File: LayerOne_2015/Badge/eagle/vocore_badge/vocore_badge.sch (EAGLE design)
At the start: 19 parts

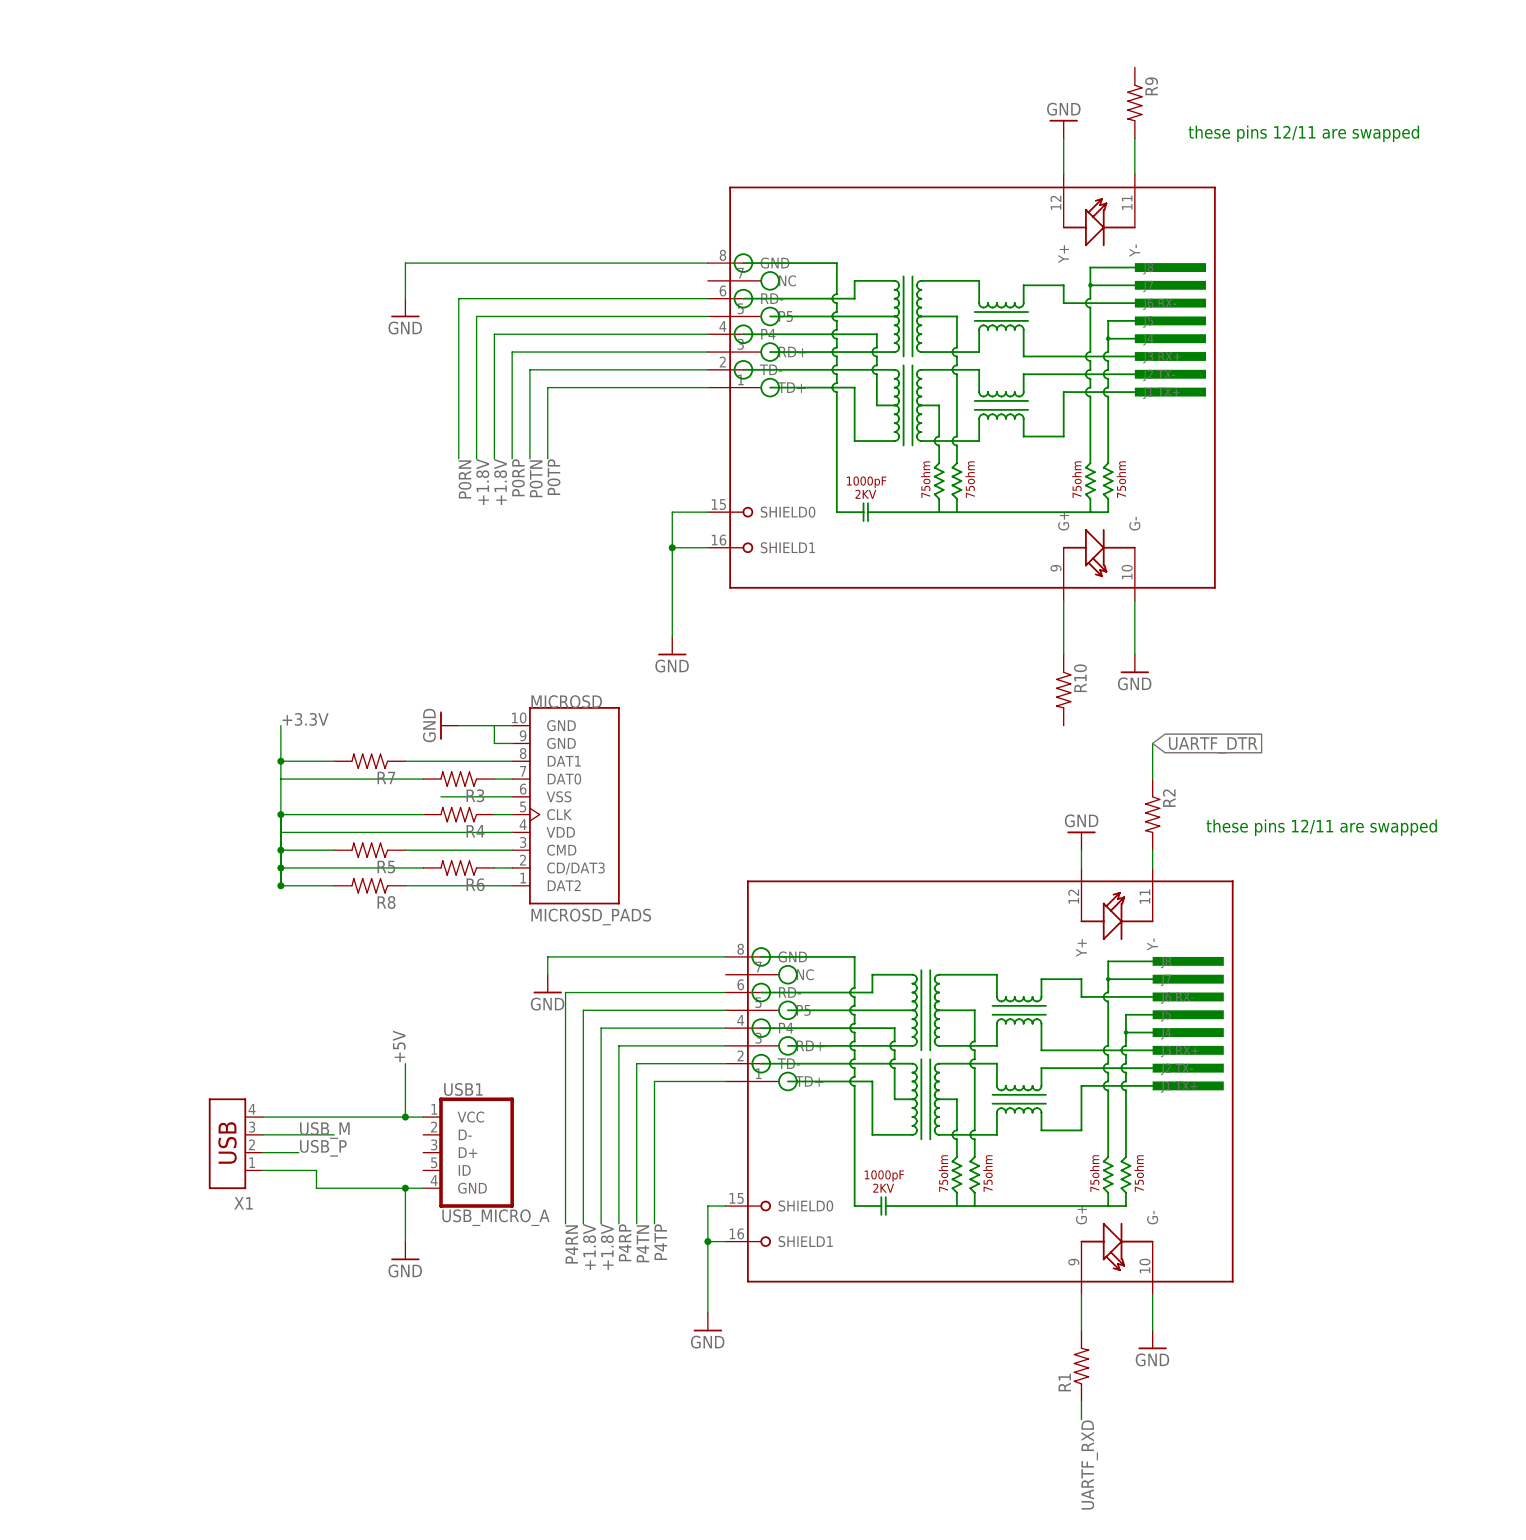
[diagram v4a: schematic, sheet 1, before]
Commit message: elongated pads on 245 logic convertor
fixed usb on badge
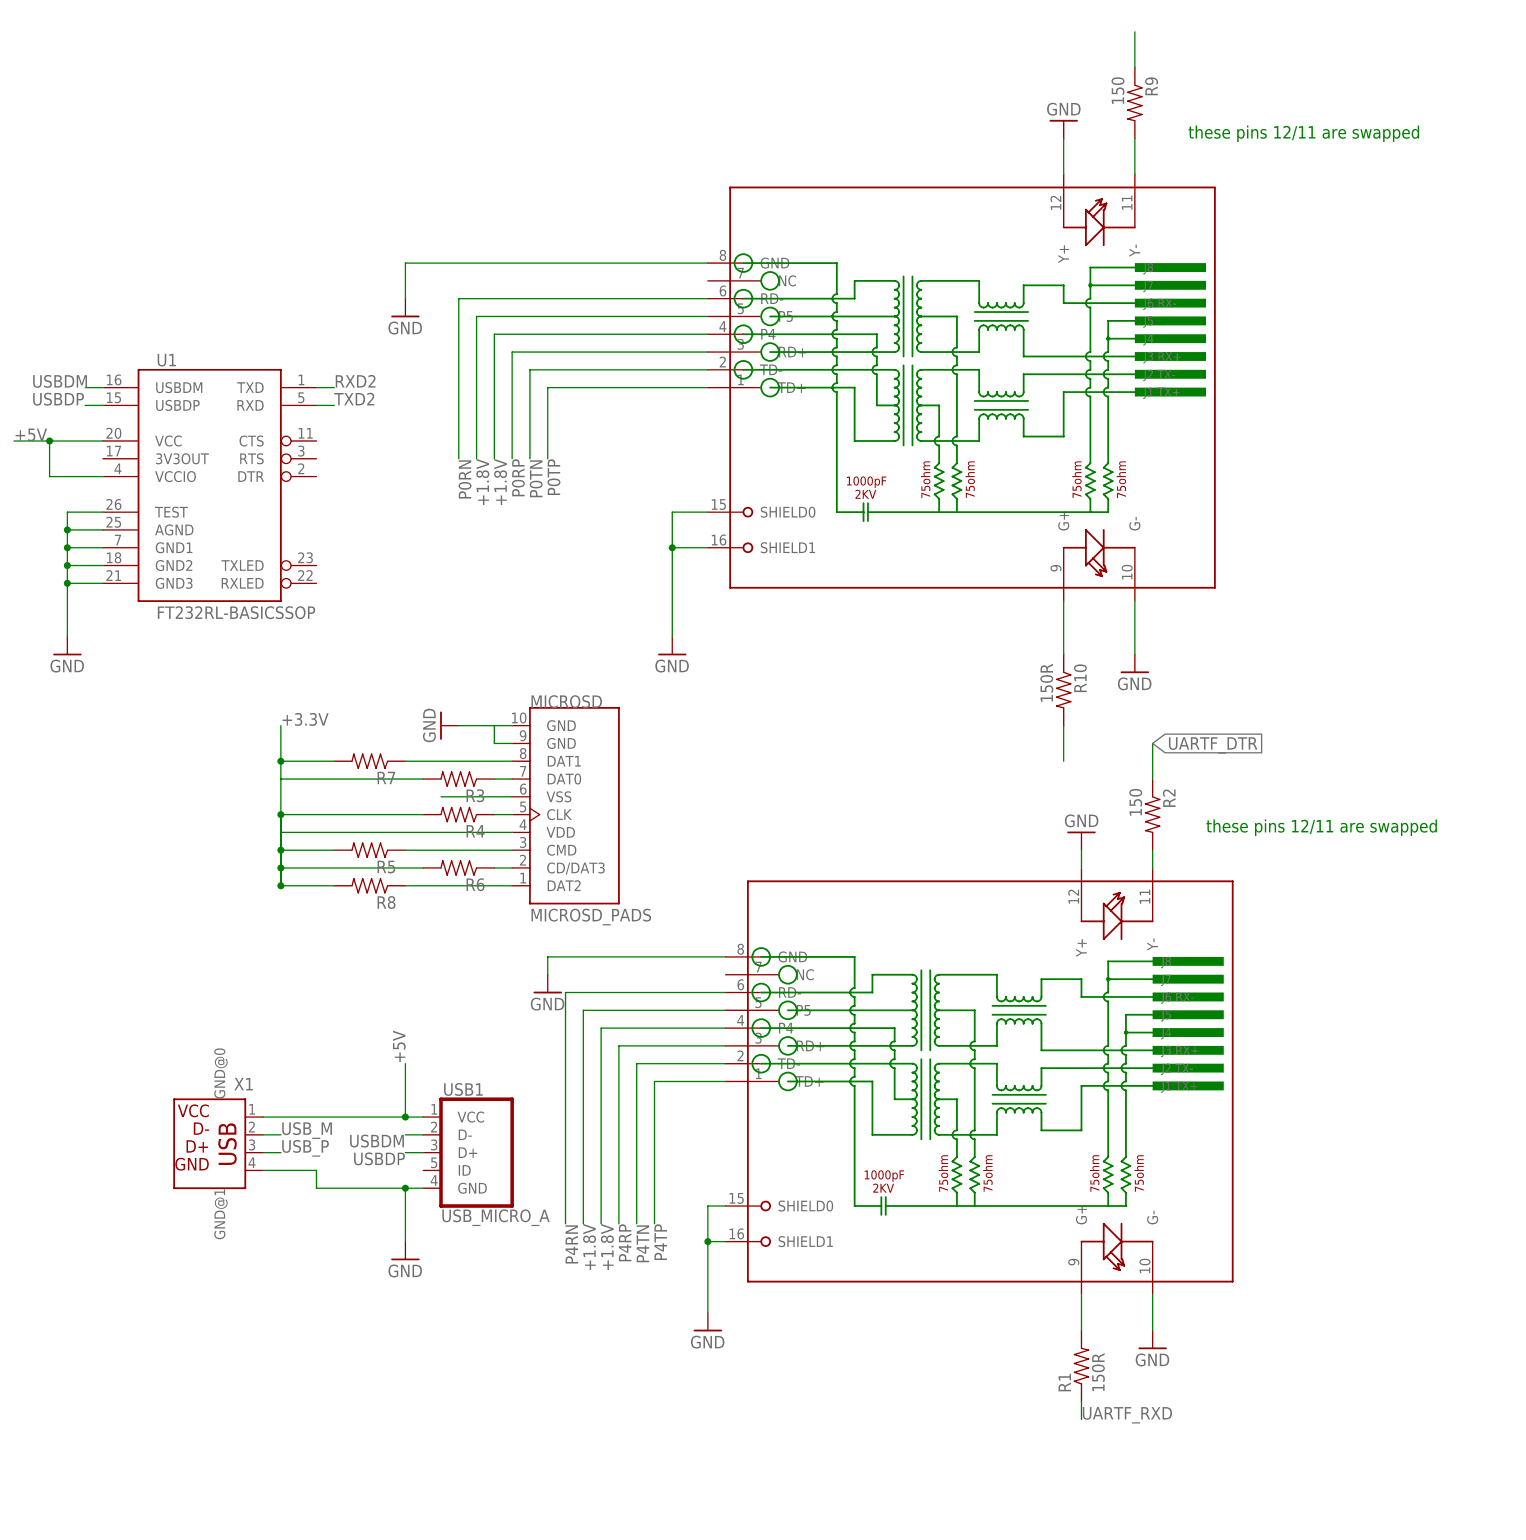
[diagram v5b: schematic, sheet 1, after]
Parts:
- added JP4: (no value), adafruit:PINHD-1X3
- added JP5: (no value), pinhead:PINHD-1X2
- added U1: FT232RL-BASICSSOP, SparkFun:FT232RL-BASICSSOP
- R1, R10: value (none) -> 150R
- R2, R9: value (none) -> 150
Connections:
- new net N$6: R9.1
- new net N$7: R10.2
- new net USBDM: U1.USBDM, USB1.D-
- new net USBDP: U1.USBDP, USB1.D+
- net +5V: now also JP5.2, U1.VCC, U1.VCCIO, X1.1; no longer X1.4
- net GND: now also JP4.1, JP5.1, U1.AGND, U1.GND1, U1.GND2, U1.GND3, U1.TEST, X1.4; no longer X1.1
- net RXD2: now also JP4.2, U1.TXD
- net TXD2: now also JP4.3, U1.RXD
- net USB_M: now also X1.2; no longer X1.3
- net USB_P: now also X1.3; no longer X1.2
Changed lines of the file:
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@@
 <classes>
 <class number="0" name="default" width="0.254" drill="0">
+<clearance class="0" value="0.1524"/>
 </class>
 </classes>
@@
 <part name="GND2" library="supply1" deviceset="GND" device=""/>
 <part name="GND3" library="supply1" deviceset="GND" device=""/>
-<part name="R1" library="SparkFun-Resistors" deviceset="RESISTOR" device="0805-RES"/>
-<part name="R2" library="SparkFun-Resistors" deviceset="RESISTOR" device="0805-RES"/>
+<part name="R1" library="SparkFun-Resistors" deviceset="RESISTOR" device="0805-RES" value="150R"/>
+<part name="R2" library="SparkFun-Resistors" deviceset="RESISTOR" device="0805-RES" value="150"/>
 <part name="R3" library="SparkFun-Resistors" deviceset="RESISTOR" device="0805-RES"/>
 <part name="R4" library="SparkFun-Resistors" deviceset="RESISTOR" device="0805-RES"/>
@@
 <part name="GND10" library="supply1" deviceset="GND" device=""/>
 <part name="GND11" library="supply1" deviceset="GND" device=""/>
-<part name="R9" library="SparkFun-Resistors" deviceset="RESISTOR" device="0805-RES"/>
-<part name="R10" library="SparkFun-Resistors" deviceset="RESISTOR" device="0805-RES"/>
-<part name="X1" library="con-amp" deviceset="USB-787616" device=""/>
+<part name="R9" library="SparkFun-Resistors" deviceset="RESISTOR" device="0805-RES" value="150"/>
+<part name="R10" library="SparkFun-Resistors" deviceset="RESISTOR" device="0805-RES" value="150R"/>
 <part name="JP1" library="adafruit" deviceset="PINHD-1X14" device=""/>
 <part name="JP2" library="adafruit" deviceset="PINHD-1X14" device=""/>
 <part name="JP3" library="microbuilder" deviceset="HEADER-1X7" device="ROUND"/>
+<part name="U1" library="SparkFun" deviceset="FT232RL-BASIC" device="SSOP"/>
+<part name="GND12" library="supply1" deviceset="GND" device=""/>
+<part name="JP4" library="adafruit" deviceset="PINHD-1X3" device=""/>
+<part name="JP5" library="pinhead" deviceset="PINHD-1X2" device=""/>
+<part name="X1" library="con-amp" deviceset="USB-787616" device=""/>
 </parts>
 <sheets>
@@
 <instance part="R9" gate="G$1" x="-93.98" y="226.06" rot="R270"/>
 <instance part="R10" gate="G$1" x="-104.14" y="142.24" rot="R270"/>
-<instance part="X1" gate="G$1" x="-223.52" y="78.74" rot="R180"/>
+<instance part="U1" gate="G$1" x="-226.06" y="172.72"/>
+<instance part="GND12" gate="1" x="-246.38" y="147.32"/>
+<instance part="X1" gate="G$1" x="-223.52" y="76.2" rot="MR0"/>
 </instances>
 <busses>
@@
 <wire x1="-210.82" y1="71.12" x2="-210.82" y2="73.66" width="0.1524" layer="91"/>
 <junction x="-198.12" y="71.12"/>
-<pinref part="X1" gate="G$1" pin="1"/>
+<pinref part="X1" gate="G$1" pin="4"/>
 </segment>
 <segment>
@@
 <pinref part="GND11" gate="1" pin="GND"/>
 </segment>
+<segment>
+<pinref part="U1" gate="G$1" pin="GND1"/>
+<wire x1="-241.3" y1="162.56" x2="-246.38" y2="162.56" width="0.1524" layer="91"/>
+<wire x1="-246.38" y1="162.56" x2="-246.38" y2="160.02" width="0.1524" layer="91"/>
+<pinref part="U1" gate="G$1" pin="GND2"/>
+<wire x1="-246.38" y1="160.02" x2="-246.38" y2="157.48" width="0.1524" layer="91"/>
+<wire x1="-246.38" y1="157.48" x2="-246.38" y2="149.86" width="0.1524" layer="91"/>
+<wire x1="-241.3" y1="160.02" x2="-246.38" y2="160.02" width="0.1524" layer="91"/>
+<pinref part="U1" gate="G$1" pin="GND3"/>
+<wire x1="-241.3" y1="157.48" x2="-246.38" y2="157.48" width="0.1524" layer="91"/>
+<junction x="-246.38" y="157.48"/>
+<junction x="-246.38" y="160.02"/>
+<pinref part="U1" gate="G$1" pin="AGND"/>
+<wire x1="-241.3" y1="165.1" x2="-246.38" y2="165.1" width="0.1524" layer="91"/>
+<wire x1="-246.38" y1="165.1" x2="-246.38" y2="162.56" width="0.1524" layer="91"/>
+<pinref part="GND12" gate="1" pin="GND"/>
+<pinref part="U1" gate="G$1" pin="TEST"/>
+<wire x1="-241.3" y1="167.64" x2="-246.38" y2="167.64" width="0.1524" layer="91"/>
+<wire x1="-246.38" y1="167.64" x2="-246.38" y2="165.1" width="0.1524" layer="91"/>
+<junction x="-246.38" y="162.56"/>
+<junction x="-246.38" y="165.1"/>
+</segment>
 </net>
 <net name="LED_G" class="0">
@@
 <pinref part="R1" gate="G$1" pin="1"/>
 <wire x1="-101.6" y1="40.64" x2="-101.6" y2="38.1" width="0.1524" layer="91"/>
-<label x="-101.6" y="38.1" size="1.778" layer="95" rot="R270"/>
+<label x="-101.6" y="38.1" size="1.778" layer="95"/>
 </segment>
 </net>
@@
 <wire x1="-218.44" y1="81.28" x2="-198.12" y2="81.28" width="0.1524" layer="91"/>
 <junction x="-198.12" y="81.28"/>
-<pinref part="X1" gate="G$1" pin="4"/>
+<pinref part="X1" gate="G$1" pin="1"/>
+</segment>
+<segment>
+<pinref part="U1" gate="G$1" pin="VCCIO"/>
+<wire x1="-241.3" y1="172.72" x2="-248.92" y2="172.72" width="0.1524" layer="91"/>
+<wire x1="-248.92" y1="172.72" x2="-248.92" y2="177.8" width="0.1524" layer="91"/>
+<pinref part="U1" gate="G$1" pin="VCC"/>
+<wire x1="-248.92" y1="177.8" x2="-254" y2="177.8" width="0.1524" layer="91"/>
+<wire x1="-241.3" y1="177.8" x2="-248.92" y2="177.8" width="0.1524" layer="91"/>
+<junction x="-248.92" y="177.8"/>
+<label x="-254" y="177.8" size="1.778" layer="95"/>
 </segment>
 </net>
 <net name="USB_P" class="0">
 <segment>
-<wire x1="-218.44" y1="76.2" x2="-213.36" y2="76.2" width="0.1524" layer="91"/>
-<label x="-213.36" y="76.2" size="1.778" layer="95"/>
+<wire x1="-218.44" y1="76.2" x2="-215.9" y2="76.2" width="0.1524" layer="91"/>
+<label x="-215.9" y="76.2" size="1.778" layer="95"/>
+<pinref part="X1" gate="G$1" pin="3"/>
+</segment>
+</net>
+<net name="USB_M" class="0">
+<segment>
+<wire x1="-218.44" y1="78.74" x2="-215.9" y2="78.74" width="0.1524" layer="91"/>
+<label x="-215.9" y="78.74" size="1.778" layer="95"/>
 <pinref part="X1" gate="G$1" pin="2"/>
-</segment>
-</net>
-<net name="USB_M" class="0">
-<segment>
-<wire x1="-218.44" y1="78.74" x2="-208.28" y2="78.74" width="0.1524" layer="91"/>
-<label x="-213.36" y="78.74" size="1.778" layer="95"/>
-<pinref part="X1" gate="G$1" pin="3"/>
 </segment>
 </net>
@@
 </segment>
 </net>
+<net name="USBDM" class="0">
+<segment>
+<pinref part="USB1" gate="G$1" pin="D-"/>
+<wire x1="-195.58" y1="78.74" x2="-198.12" y2="78.74" width="0.1524" layer="91"/>
+<label x="-198.12" y="78.74" size="1.778" layer="95" rot="R180"/>
+</segment>
+<segment>
+<wire x1="-241.3" y1="185.42" x2="-243.84" y2="185.42" width="0.1524" layer="91"/>
+<pinref part="U1" gate="G$1" pin="USBDM"/>
+<label x="-251.46" y="185.42" size="1.778" layer="95"/>
+</segment>
+</net>
+<net name="USBDP" class="0">
+<segment>
+<pinref part="USB1" gate="G$1" pin="D+"/>
+<wire x1="-195.58" y1="76.2" x2="-198.12" y2="76.2" width="0.1524" layer="91"/>
+<label x="-198.12" y="76.2" size="1.778" layer="95" rot="R180"/>
+</segment>
+<segment>
+<wire x1="-241.3" y1="182.88" x2="-243.84" y2="182.88" width="0.1524" layer="91"/>
+<pinref part="U1" gate="G$1" pin="USBDP"/>
+<label x="-251.46" y="182.88" size="1.778" layer="95"/>
+</segment>
+</net>
+<net name="RXD2" class="0">
+<segment>
+<pinref part="U1" gate="G$1" pin="TXD"/>
+<wire x1="-210.82" y1="185.42" x2="-208.28" y2="185.42" width="0.1524" layer="91"/>
+<label x="-208.28" y="185.42" size="1.778" layer="95"/>
+</segment>
+</net>
+<net name="TXD2" class="0">
+<segment>
+<pinref part="U1" gate="G$1" pin="RXD"/>
+<wire x1="-210.82" y1="182.88" x2="-208.28" y2="182.88" width="0.1524" layer="91"/>
+<label x="-208.28" y="182.88" size="1.778" layer="95"/>
+</segment>
+</net>
+<net name="N$6" class="0">
+<segment>
+<pinref part="R9" gate="G$1" pin="1"/>
+<wire x1="-93.98" y1="231.14" x2="-93.98" y2="236.22" width="0.1524" layer="91"/>
+</segment>
+</net>
+<net name="N$7" class="0">
+<segment>
+<pinref part="R10" gate="G$1" pin="2"/>
+<wire x1="-104.14" y1="137.16" x2="-104.14" y2="132.08" width="0.1524" layer="91"/>
+</segment>
+</net>
 </nets>
 </sheet>
@@
 <instance part="JP2" gate="A" x="154.94" y="20.32"/>
 <instance part="JP3" gate="A" x="137.16" y="45.72"/>
+<instance part="JP4" gate="A" x="91.44" y="-7.62" rot="R270"/>
+<instance part="JP5" gate="G$1" x="63.5" y="-7.62" rot="R270"/>
 </instances>
 <busses>
@@
 <pinref part="JP3" gate="A" pin="7"/>
 </segment>
+<segment>
+<pinref part="JP4" gate="A" pin="1"/>
+<wire x1="93.98" y1="-5.08" x2="93.98" y2="5.08" width="0.1524" layer="91"/>
+<label x="93.98" y="5.08" size="1.778" layer="95" rot="R90"/>
+</segment>
+<segment>
+<pinref part="JP5" gate="G$1" pin="1"/>
+<wire x1="66.04" y1="-5.08" x2="66.04" y2="7.62" width="0.1524" layer="91"/>
+<label x="66.04" y="7.62" size="1.778" layer="95" rot="R90"/>
+</segment>
 </net>
 <net name="P4RN" class="0">
@@
 <label x="33.02" y="27.94" size="1.778" layer="95"/>
 </segment>
+<segment>
+<pinref part="JP5" gate="G$1" pin="2"/>
+<wire x1="63.5" y1="-5.08" x2="63.5" y2="7.62" width="0.1524" layer="91"/>
+<label x="63.5" y="7.62" size="1.778" layer="95" rot="R90"/>
+</segment>
 </net>
 <net name="UARTF_DTR" class="0">
@@
 <label x="116.84" y="35.56" size="1.778" layer="95"/>
 </segment>
+<segment>
+<pinref part="JP4" gate="A" pin="3"/>
+<wire x1="88.9" y1="-5.08" x2="88.9" y2="5.08" width="0.1524" layer="91"/>
+<label x="88.9" y="5.08" size="1.778" layer="95" rot="R90"/>
+</segment>
 </net>
 <net name="RXD2" class="0">
@@
 <label x="116.84" y="33.02" size="1.778" layer="95"/>
 </segment>
-</net>
+<segment>
+<pinref part="JP4" gate="A" pin="2"/>
+<wire x1="91.44" y1="-5.08" x2="91.44" y2="5.08" width="0.1524" layer="91"/>
+<label x="91.44" y="5.08" size="1.778" layer="95" rot="R90"/>
+</segment>
+</net>

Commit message: whoops. crossing track fixed.
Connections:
- removed net N$6: R9.1
- removed net N$7: R10.2
- net LED1: now also R10.2
- net LED2: now also R9.1
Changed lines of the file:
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@@
 </segment>
 </net>
-<net name="N$6" class="0">
+<net name="LED2" class="0">
 <segment>
 <pinref part="R9" gate="G$1" pin="1"/>
@@
 </segment>
 </net>
-<net name="N$7" class="0">
+<net name="LED1" class="0">
 <segment>
 <pinref part="R10" gate="G$1" pin="2"/>
